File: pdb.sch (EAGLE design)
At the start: 38 parts, among them Q1 20MHz, Q2 IRFR5305PBF, Q3 IRFR5305PBF, U1 TSR_1-2433, U2 LTC2946CMSPBF, U3 LTC2946CMSPBF, U4 LTC2946CMSPBF, U5 ATMEGA48-20AU, U6 TXB0104, U7 AT30TS74SS8M

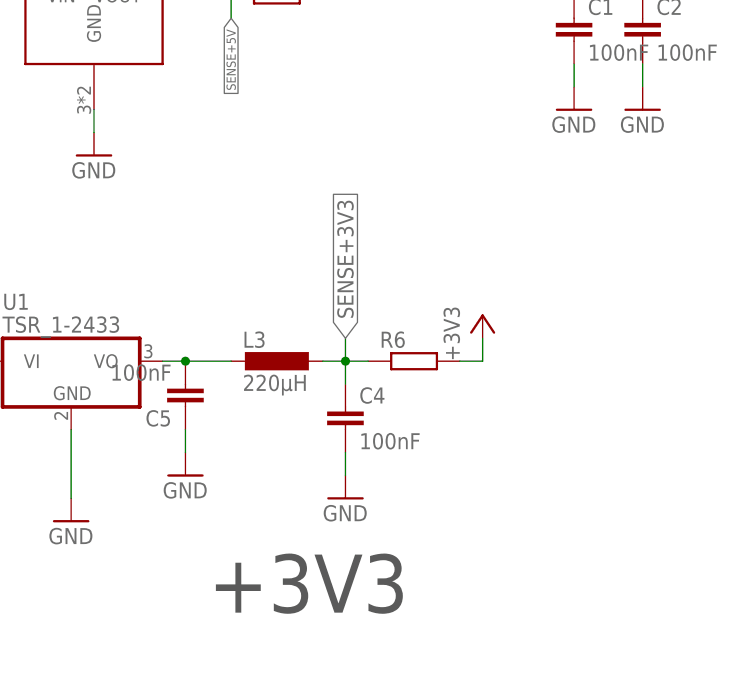
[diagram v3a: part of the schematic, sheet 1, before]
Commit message: updated inductor for 3v regulator
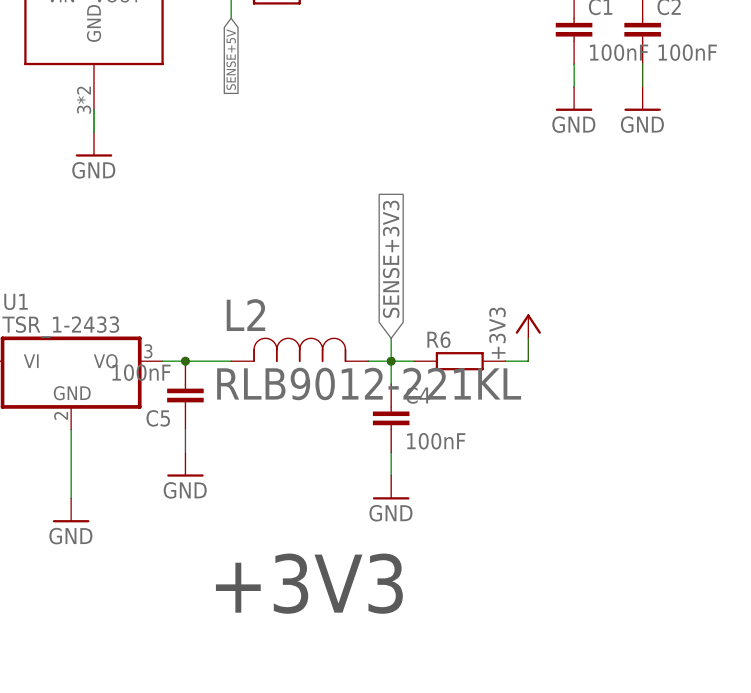
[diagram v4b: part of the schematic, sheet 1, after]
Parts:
- removed L3: 220µH, resistor:L-EU0207/7
- added L2: RLB9012-221KL, jonas_bourns:RLB9012-221KL
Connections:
- net N$6: now also L2.2; no longer L3.2
- net SENSE+3V3: now also L2.1; no longer L3.1
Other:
- moved on the sheet: C4, R6
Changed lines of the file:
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@@
 <part name="C1" library="rcl" library_urn="urn:adsk.eagle:library:334" deviceset="C-EU" device="C0603" package3d_urn="urn:adsk.eagle:package:23616/2" value="100nF"/>
 <part name="C2" library="rcl" library_urn="urn:adsk.eagle:library:334" deviceset="C-EU" device="C0603" package3d_urn="urn:adsk.eagle:package:23616/2" value="100nF"/>
-<part name="L3" library="resistor" deviceset="L-EU" device="0207/7" value="220µH"/>
 <part name="C4" library="resistor" deviceset="C-EU" device="C0603" value="100nF"/>
 <part name="C5" library="resistor" deviceset="C-EU" device="C0603" value="100nF"/>
@@
 <part name="FRAME4" library="frames" library_urn="urn:adsk.eagle:library:229" deviceset="A3L-LOC" device=""/>
 <part name="U7" library="jonas_microchip" library_urn="urn:adsk.eagle:library:891228" deviceset="AT30TS74" device="SS8M" package3d_urn="urn:adsk.eagle:package:1422804/3"/>
+<part name="L2" library="jonas_bourns" library_urn="urn:adsk.eagle:library:1422904" deviceset="RLB9012-221KL" device="" package3d_urn="urn:adsk.eagle:package:1422907/3"/>
 </parts>
 <sheets>
@@
 <instance part="C1" gate="G$1" x="58.42" y="53.34"/>
 <instance part="C2" gate="G$1" x="66.04" y="53.34"/>
-<instance part="L3" gate="G$1" x="25.4" y="15.24" rot="R270"/>
-<instance part="C4" gate="G$1" x="33.02" y="10.16"/>
+<instance part="C4" gate="G$1" x="38.1" y="10.16"/>
 <instance part="C5" gate="G$1" x="15.24" y="10.16" rot="R180"/>
 <instance part="GND17" gate="1" x="2.54" y="-2.54"/>
-<instance part="GND19" gate="1" x="33.02" y="0"/>
+<instance part="GND19" gate="1" x="38.1" y="0"/>
 <instance part="GND15" gate="1" x="15.24" y="2.54"/>
-<instance part="+3V2" gate="G$1" x="48.26" y="20.32"/>
+<instance part="+3V2" gate="G$1" x="53.34" y="20.32"/>
 <instance part="U1" gate="G$1" x="2.54" y="15.24"/>
 <instance part="SUPPLY6" gate="1" x="-12.7" y="20.32"/>
@@
 <instance part="R4" gate="G$1" x="-27.94" y="55.88"/>
 <instance part="R5" gate="G$1" x="25.4" y="55.88"/>
-<instance part="R6" gate="G$1" x="40.64" y="15.24"/>
+<instance part="R6" gate="G$1" x="45.72" y="15.24"/>
 <instance part="FRAME3" gate="G$1" x="-127" y="-50.8"/>
 <instance part="ESC" gate="G$1" x="-99.06" y="-17.78" rot="MR0"/>
 <instance part="GND18" gate="1" x="-86.36" y="-25.4"/>
 <instance part="SUPPLY17" gate="1" x="-86.36" y="-10.16"/>
+<instance part="L2" gate="A" x="20.32" y="15.24"/>
 </instances>
 <busses>
@@
 <segment>
 <pinref part="C4" gate="G$1" pin="2"/>
-<wire x1="33.02" y1="2.54" x2="33.02" y2="5.08" width="0.1524" layer="91"/>
+<wire x1="38.1" y1="2.54" x2="38.1" y2="5.08" width="0.1524" layer="91"/>
 <pinref part="GND19" gate="1" pin="GND"/>
 </segment>
@@
 <net name="N$6" class="0">
 <segment>
-<pinref part="L3" gate="G$1" pin="2"/>
 <pinref part="C5" gate="G$1" pin="2"/>
 <wire x1="15.24" y1="15.24" x2="20.32" y2="15.24" width="0.1524" layer="91"/>
@@
 <junction x="15.24" y="15.24"/>
 <wire x1="15.24" y1="15.24" x2="12.7" y2="15.24" width="0.1524" layer="91"/>
+<pinref part="L2" gate="A" pin="2"/>
 </segment>
 </net>
@@
 <net name="SENSE+3V3" class="0">
 <segment>
-<wire x1="33.02" y1="15.24" x2="33.02" y2="12.7" width="0.1524" layer="91"/>
+<wire x1="38.1" y1="15.24" x2="38.1" y2="12.7" width="0.1524" layer="91"/>
 <pinref part="C4" gate="G$1" pin="1"/>
 <pinref part="R6" gate="G$1" pin="1"/>
-<wire x1="33.02" y1="15.24" x2="35.56" y2="15.24" width="0.1524" layer="91"/>
-<pinref part="L3" gate="G$1" pin="1"/>
-<wire x1="30.48" y1="15.24" x2="33.02" y2="15.24" width="0.1524" layer="91"/>
-<junction x="33.02" y="15.24"/>
-<wire x1="33.02" y1="15.24" x2="33.02" y2="17.78" width="0.1524" layer="91"/>
-<label x="33.02" y="17.78" size="1.778" layer="95" rot="R90" xref="yes"/>
+<wire x1="38.1" y1="15.24" x2="40.64" y2="15.24" width="0.1524" layer="91"/>
+<wire x1="35.56" y1="15.24" x2="38.1" y2="15.24" width="0.1524" layer="91"/>
+<junction x="38.1" y="15.24"/>
+<wire x1="38.1" y1="15.24" x2="38.1" y2="17.78" width="0.1524" layer="91"/>
+<label x="38.1" y="17.78" size="1.778" layer="95" rot="R90" xref="yes"/>
+<pinref part="L2" gate="A" pin="1"/>
 </segment>
 </net>
@@
 <segment>
 <pinref part="R6" gate="G$1" pin="2"/>
-<wire x1="45.72" y1="15.24" x2="48.26" y2="15.24" width="0.1524" layer="91"/>
-<wire x1="48.26" y1="15.24" x2="48.26" y2="17.78" width="0.1524" layer="91"/>
+<wire x1="50.8" y1="15.24" x2="53.34" y2="15.24" width="0.1524" layer="91"/>
+<wire x1="53.34" y1="15.24" x2="53.34" y2="17.78" width="0.1524" layer="91"/>
 <pinref part="+3V2" gate="G$1" pin="+3V3"/>
 </segment>

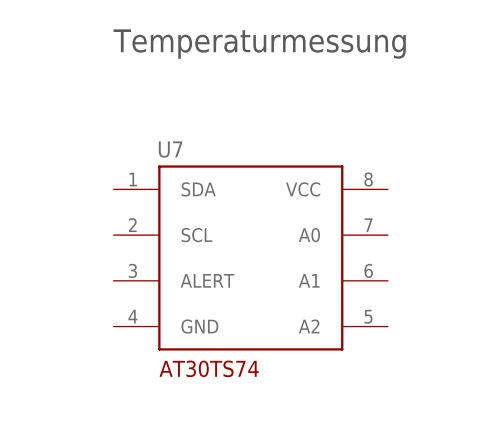
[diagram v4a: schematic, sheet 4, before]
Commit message: AT30TS74 connected
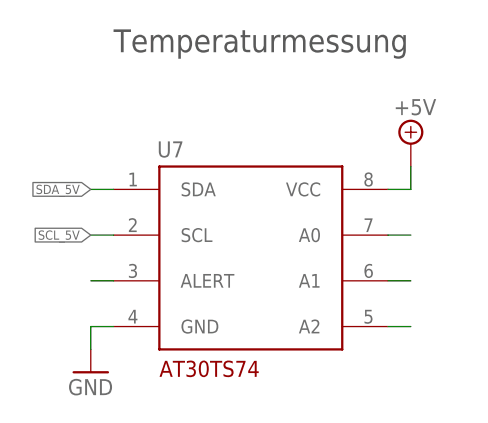
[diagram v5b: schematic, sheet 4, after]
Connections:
- new net N$11: U7.ALERT
- new net N$13: U7.A2
- new net N$14: U7.A1
- new net N$16: U7.A0
- new net SCL_5V: U7.SCL
- new net SDA_5V: U7.SDA
- net +5V: now also U7.VCC
- net GND: now also U7.GND
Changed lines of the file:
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@@
 <part name="U7" library="jonas_microchip" library_urn="urn:adsk.eagle:library:891228" deviceset="AT30TS74" device="SS8M" package3d_urn="urn:adsk.eagle:package:1422804/3"/>
 <part name="L2" library="jonas_bourns" library_urn="urn:adsk.eagle:library:1422904" deviceset="RLB9012-221KL" device="" package3d_urn="urn:adsk.eagle:package:1422907/3"/>
+<part name="SUPPLY18" library="supply2" library_urn="urn:adsk.eagle:library:372" deviceset="+5V" device=""/>
+<part name="GND20" library="supply1" library_urn="urn:adsk.eagle:library:371" deviceset="GND" device=""/>
 </parts>
 <sheets>
@@
 </segment>
 </net>
-<net name="V+" class="0">
+<net name="V+" class="2">
 <segment>
 <pinref part="SUPPLY1" gate="1" pin="V+"/>
@@
 </segment>
 </net>
-<net name="V+" class="0">
+<net name="V+" class="2">
 <segment>
 <pinref part="SUPPLY7" gate="1" pin="V+"/>
@@
 </segment>
 </net>
-<net name="V+" class="0">
+<net name="V+" class="2">
 <segment>
 <pinref part="U2" gate="A" pin="VDD"/>
@@
 <instance part="FRAME4" gate="G$1" x="0" y="0"/>
 <instance part="U7" gate="IC1" x="124.46" y="142.24"/>
+<instance part="SUPPLY18" gate="+5V" x="142.24" y="154.94"/>
+<instance part="GND20" gate="1" x="106.68" y="129.54"/>
 </instances>
 <busses>
 </busses>
 <nets>
+<net name="SDA_5V" class="0">
+<segment>
+<pinref part="U7" gate="IC1" pin="SDA"/>
+<wire x1="109.22" y1="149.86" x2="106.68" y2="149.86" width="0.1524" layer="91"/>
+<label x="106.68" y="149.86" size="1.016" layer="95" rot="R180" xref="yes"/>
+</segment>
+</net>
+<net name="SCL_5V" class="0">
+<segment>
+<pinref part="U7" gate="IC1" pin="SCL"/>
+<wire x1="109.22" y1="144.78" x2="106.68" y2="144.78" width="0.1524" layer="91"/>
+<label x="106.68" y="144.78" size="1.016" layer="95" rot="R180" xref="yes"/>
+</segment>
+</net>
+<net name="N$11" class="0">
+<segment>
+<pinref part="U7" gate="IC1" pin="ALERT"/>
+<wire x1="109.22" y1="139.7" x2="106.68" y2="139.7" width="0.1524" layer="91"/>
+</segment>
+</net>
+<net name="N$13" class="0">
+<segment>
+<pinref part="U7" gate="IC1" pin="A2"/>
+<wire x1="139.7" y1="134.62" x2="142.24" y2="134.62" width="0.1524" layer="91"/>
+</segment>
+</net>
+<net name="N$14" class="0">
+<segment>
+<pinref part="U7" gate="IC1" pin="A1"/>
+<wire x1="139.7" y1="139.7" x2="142.24" y2="139.7" width="0.1524" layer="91"/>
+</segment>
+</net>
+<net name="N$16" class="0">
+<segment>
+<pinref part="U7" gate="IC1" pin="A0"/>
+<wire x1="139.7" y1="144.78" x2="142.24" y2="144.78" width="0.1524" layer="91"/>
+</segment>
+</net>
+<net name="+5V" class="0">
+<segment>
+<pinref part="U7" gate="IC1" pin="VCC"/>
+<wire x1="139.7" y1="149.86" x2="142.24" y2="149.86" width="0.1524" layer="91"/>
+<wire x1="142.24" y1="149.86" x2="142.24" y2="152.4" width="0.1524" layer="91"/>
+<pinref part="SUPPLY18" gate="+5V" pin="+5V"/>
+</segment>
+</net>
+<net name="GND" class="0">
+<segment>
+<pinref part="U7" gate="IC1" pin="GND"/>
+<wire x1="109.22" y1="134.62" x2="106.68" y2="134.62" width="0.1524" layer="91"/>
+<wire x1="106.68" y1="134.62" x2="106.68" y2="132.08" width="0.1524" layer="91"/>
+<pinref part="GND20" gate="1" pin="GND"/>
+</segment>
+</net>
 </nets>
 </sheet>

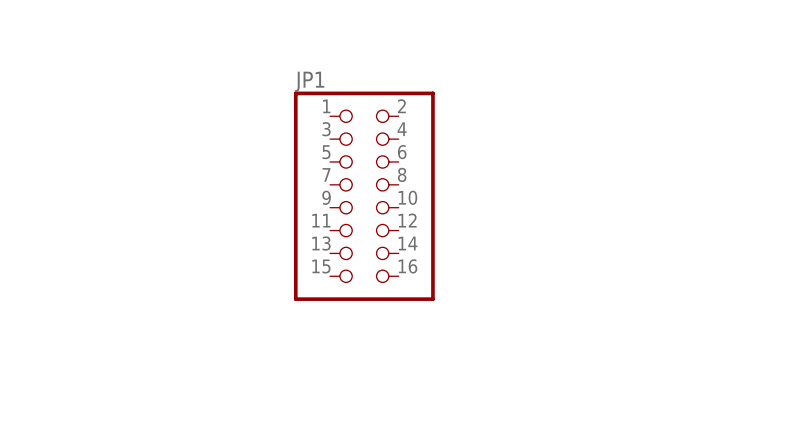
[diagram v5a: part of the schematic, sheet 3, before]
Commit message: Header connected, First Layout attempt
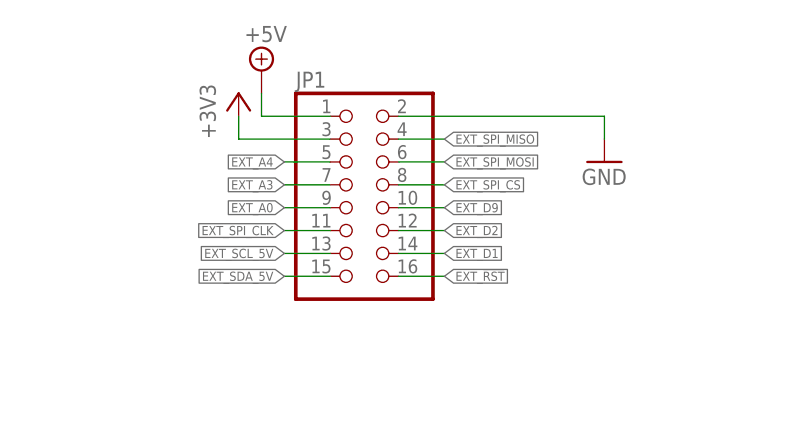
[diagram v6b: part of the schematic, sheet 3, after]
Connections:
- removed net MISO_3V3: U6.A1
- removed net MOSI_3V3: U6.A2
- removed net SS_3V3: U6.A4
- new net EXT_!RST: JP1.16
- new net EXT_A0: JP1.9
- new net EXT_A3: JP1.7
- new net EXT_A4: JP1.5
- new net EXT_D1: JP1.14
- new net EXT_D2: JP1.12
- new net EXT_D9: JP1.10
- new net EXT_SCL_5V: JP1.13
- new net EXT_SDA_5V: JP1.15
- new net EXT_SPI_CLK: JP1.11, U6.A3
- new net EXT_SPI_CS: JP1.8, U6.A4
- new net EXT_SPI_MISO: JP1.4, U6.A2
- new net EXT_SPI_MOSI: JP1.6, U6.A1
- net +3V3: now also JP1.3
- net +5V: now also JP1.1
- net GND: now also JP1.2
- net SCK_5V: no longer U6.A3
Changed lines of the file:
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@@
 <part name="SUPPLY18" library="supply2" library_urn="urn:adsk.eagle:library:372" deviceset="+5V" device=""/>
 <part name="GND20" library="supply1" library_urn="urn:adsk.eagle:library:371" deviceset="GND" device=""/>
+<part name="GND21" library="supply1" library_urn="urn:adsk.eagle:library:371" deviceset="GND" device=""/>
+<part name="SUPPLY19" library="supply2" library_urn="urn:adsk.eagle:library:372" deviceset="+5V" device=""/>
+<part name="+3V5" library="supply1" library_urn="urn:adsk.eagle:library:371" deviceset="+3V3" device=""/>
 </parts>
 <sheets>
@@
 </segment>
 <segment>
-<pinref part="U6" gate="G$1" pin="A3"/>
-<wire x1="25.4" y1="81.28" x2="22.86" y2="81.28" width="0.1524" layer="91"/>
-<label x="22.86" y="81.28" size="1.016" layer="95" rot="R180" xref="yes"/>
-</segment>
-<segment>
 <pinref part="U6" gate="G$1" pin="B3"/>
 <wire x1="55.88" y1="81.28" x2="58.42" y2="81.28" width="0.1524" layer="91"/>
@@
 </segment>
 </net>
-<net name="MISO_3V3" class="0">
+<net name="EXT_SPI_MOSI" class="0">
 <segment>
 <pinref part="U6" gate="G$1" pin="A1"/>
@@
 </segment>
 </net>
-<net name="MOSI_3V3" class="0">
+<net name="EXT_SPI_MISO" class="0">
 <segment>
 <pinref part="U6" gate="G$1" pin="A2"/>
@@
 </segment>
 </net>
-<net name="SS_3V3" class="0">
+<net name="EXT_SPI_CS" class="0">
 <segment>
 <pinref part="U6" gate="G$1" pin="A4"/>
 <wire x1="25.4" y1="78.74" x2="22.86" y2="78.74" width="0.1524" layer="91"/>
 <label x="22.86" y="78.74" size="1.016" layer="95" rot="R180" xref="yes"/>
+</segment>
+</net>
+<net name="EXT_SPI_CLK" class="0">
+<segment>
+<pinref part="U6" gate="G$1" pin="A3"/>
+<wire x1="25.4" y1="81.28" x2="22.86" y2="81.28" width="0.1524" layer="91"/>
+<label x="22.86" y="81.28" size="1.016" layer="95" rot="R180" xref="yes"/>
 </segment>
 </net>
@@
 <instance part="FRAME1" gate="G$1" x="0" y="0"/>
 <instance part="JP1" gate="A" x="152.4" y="210.82"/>
+<instance part="GND21" gate="1" x="180.34" y="213.36"/>
+<instance part="SUPPLY19" gate="+5V" x="142.24" y="223.52"/>
+<instance part="+3V5" gate="G$1" x="139.7" y="220.98"/>
 </instances>
 <busses>
@@
 <pinref part="GND11" gate="1" pin="GND"/>
 </segment>
+<segment>
+<pinref part="JP1" gate="A" pin="2"/>
+<wire x1="157.48" y1="218.44" x2="180.34" y2="218.44" width="0.1524" layer="91"/>
+<wire x1="180.34" y1="218.44" x2="180.34" y2="215.9" width="0.1524" layer="91"/>
+<pinref part="GND21" gate="1" pin="GND"/>
+</segment>
 </net>
 <net name="V+" class="2">
@@
 <wire x1="121.92" y1="78.74" x2="121.92" y2="81.28" width="0.1524" layer="91"/>
 </segment>
+<segment>
+<pinref part="JP1" gate="A" pin="1"/>
+<wire x1="149.86" y1="218.44" x2="142.24" y2="218.44" width="0.1524" layer="91"/>
+<wire x1="142.24" y1="218.44" x2="142.24" y2="220.98" width="0.1524" layer="91"/>
+<pinref part="SUPPLY19" gate="+5V" pin="+5V"/>
+</segment>
 </net>
 <net name="+3V3" class="0">
@@
 <wire x1="238.76" y1="78.74" x2="238.76" y2="81.28" width="0.1524" layer="91"/>
 </segment>
-</net>
+<segment>
+<pinref part="JP1" gate="A" pin="3"/>
+<wire x1="149.86" y1="215.9" x2="139.7" y2="215.9" width="0.1524" layer="91"/>
+<wire x1="139.7" y1="215.9" x2="139.7" y2="218.44" width="0.1524" layer="91"/>
+<pinref part="+3V5" gate="G$1" pin="+3V3"/>
+</segment>
+</net>
+<net name="EXT_A4" class="0">
+<segment>
+<pinref part="JP1" gate="A" pin="5"/>
+<wire x1="149.86" y1="213.36" x2="144.78" y2="213.36" width="0.1524" layer="91"/>
+<label x="144.78" y="213.36" size="1.016" layer="95" rot="R180" xref="yes"/>
+</segment>
+</net>
+<net name="EXT_A3" class="0">
+<segment>
+<pinref part="JP1" gate="A" pin="7"/>
+<wire x1="149.86" y1="210.82" x2="144.78" y2="210.82" width="0.1524" layer="91"/>
+<label x="144.78" y="210.82" size="1.016" layer="95" rot="R180" xref="yes"/>
+</segment>
+</net>
+<net name="EXT_A0" class="0">
+<segment>
+<pinref part="JP1" gate="A" pin="9"/>
+<wire x1="149.86" y1="208.28" x2="144.78" y2="208.28" width="0.1524" layer="91"/>
+<label x="144.78" y="208.28" size="1.016" layer="95" rot="R180" xref="yes"/>
+</segment>
+</net>
+<net name="EXT_SPI_CLK" class="0">
+<segment>
+<pinref part="JP1" gate="A" pin="11"/>
+<wire x1="149.86" y1="205.74" x2="144.78" y2="205.74" width="0.1524" layer="91"/>
+<label x="144.78" y="205.74" size="1.016" layer="95" rot="R180" xref="yes"/>
+</segment>
+</net>
+<net name="EXT_SCL_5V" class="0">
+<segment>
+<pinref part="JP1" gate="A" pin="13"/>
+<wire x1="149.86" y1="203.2" x2="144.78" y2="203.2" width="0.1524" layer="91"/>
+<label x="144.78" y="203.2" size="1.016" layer="95" rot="R180" xref="yes"/>
+</segment>
+</net>
+<net name="EXT_SDA_5V" class="0">
+<segment>
+<pinref part="JP1" gate="A" pin="15"/>
+<wire x1="149.86" y1="200.66" x2="144.78" y2="200.66" width="0.1524" layer="91"/>
+<label x="144.78" y="200.66" size="1.016" layer="95" rot="R180" xref="yes"/>
+</segment>
+</net>
+<net name="EXT_!RST" class="0">
+<segment>
+<pinref part="JP1" gate="A" pin="16"/>
+<wire x1="157.48" y1="200.66" x2="162.56" y2="200.66" width="0.1524" layer="91"/>
+<label x="162.56" y="200.66" size="1.016" layer="95" xref="yes"/>
+</segment>
+</net>
+<net name="EXT_D1" class="0">
+<segment>
+<pinref part="JP1" gate="A" pin="14"/>
+<wire x1="157.48" y1="203.2" x2="162.56" y2="203.2" width="0.1524" layer="91"/>
+<label x="162.56" y="203.2" size="1.016" layer="95" xref="yes"/>
+</segment>
+</net>
+<net name="EXT_D2" class="0">
+<segment>
+<pinref part="JP1" gate="A" pin="12"/>
+<wire x1="157.48" y1="205.74" x2="162.56" y2="205.74" width="0.1524" layer="91"/>
+<label x="162.56" y="205.74" size="1.016" layer="95" xref="yes"/>
+</segment>
+</net>
+<net name="EXT_D9" class="0">
+<segment>
+<pinref part="JP1" gate="A" pin="10"/>
+<wire x1="157.48" y1="208.28" x2="162.56" y2="208.28" width="0.1524" layer="91"/>
+<label x="162.56" y="208.28" size="1.016" layer="95" xref="yes"/>
+</segment>
+</net>
+<net name="EXT_SPI_CS" class="0">
+<segment>
+<pinref part="JP1" gate="A" pin="8"/>
+<wire x1="157.48" y1="210.82" x2="162.56" y2="210.82" width="0.1524" layer="91"/>
+<label x="162.56" y="210.82" size="1.016" layer="95" xref="yes"/>
+</segment>
+</net>
+<net name="EXT_SPI_MOSI" class="0">
+<segment>
+<pinref part="JP1" gate="A" pin="6"/>
+<wire x1="157.48" y1="213.36" x2="162.56" y2="213.36" width="0.1524" layer="91"/>
+<label x="162.56" y="213.36" size="1.016" layer="95" xref="yes"/>
+</segment>
+</net>
+<net name="EXT_SPI_MISO" class="0">
+<segment>
+<pinref part="JP1" gate="A" pin="4"/>
+<wire x1="157.48" y1="215.9" x2="162.56" y2="215.9" width="0.1524" layer="91"/>
+<label x="162.56" y="215.9" size="1.016" layer="95" xref="yes"/>
+</segment>
+</net>
